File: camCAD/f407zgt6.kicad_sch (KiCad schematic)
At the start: 2 parts, among them J2 SWD Header, U3 STM32F407ZGTx

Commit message: miscellaneous changes
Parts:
- removed J2: SWD Header, symbol Connector:Conn_01x02_Pin
- added J2: JTAG header, symbol Connector:Conn_01x10_Pin
- added R1: R_US, symbol Device:R_US
- added SW2: SW_Push, symbol Switch:SW_Push
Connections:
- net PDR_ON is gone; now on net VDD1: U3.143 (PDR_ON)
- net BOOT0: now also R1.1, SW2.2
- net NRST: now also J2.10 (Pin_10)
- net PB3: now also J2.6 (Pin_6)
- net VDD1: now also J2.1 (Pin_1)
- net PA13: now reaches U3.105 (PA13)
- net PA13: now also J2.2 (Pin_2)
- net PA14: now reaches U3.109 (PA14)
- net PA14: now also J2.4 (Pin_4)
- net PA15: now reaches U3.110 (PA15)
- net PA15: now also J2.8 (Pin_8)
- net PA5: now reaches U3.41 (PA5)
- net PB11: now reaches U3.70 (PB11)
- net PD1: no longer names the net of U3.115 (PD1)
- net PD2: no longer names the net of U3.116 (PD2)
- new net GND: J2.3 (Pin_3), J2.5 (Pin_5), J2.9 (Pin_9), R1.2
- new net SC_3V3: SW2.1
- no-connect marks 0 -> 81
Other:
- note added: "ARM10-compatible connector (JTAG)"
- note added: "Bootloader mode switch"
- note added: "JCLK"
- note added: "JRCLK"
- note added: "JTDI"
- note added: "JTDO"
- note added: "JTMS"
- note added: "NRST"
- note added: "VCC"
- note removed: "SWCLK"
- note removed: "SWDIO"

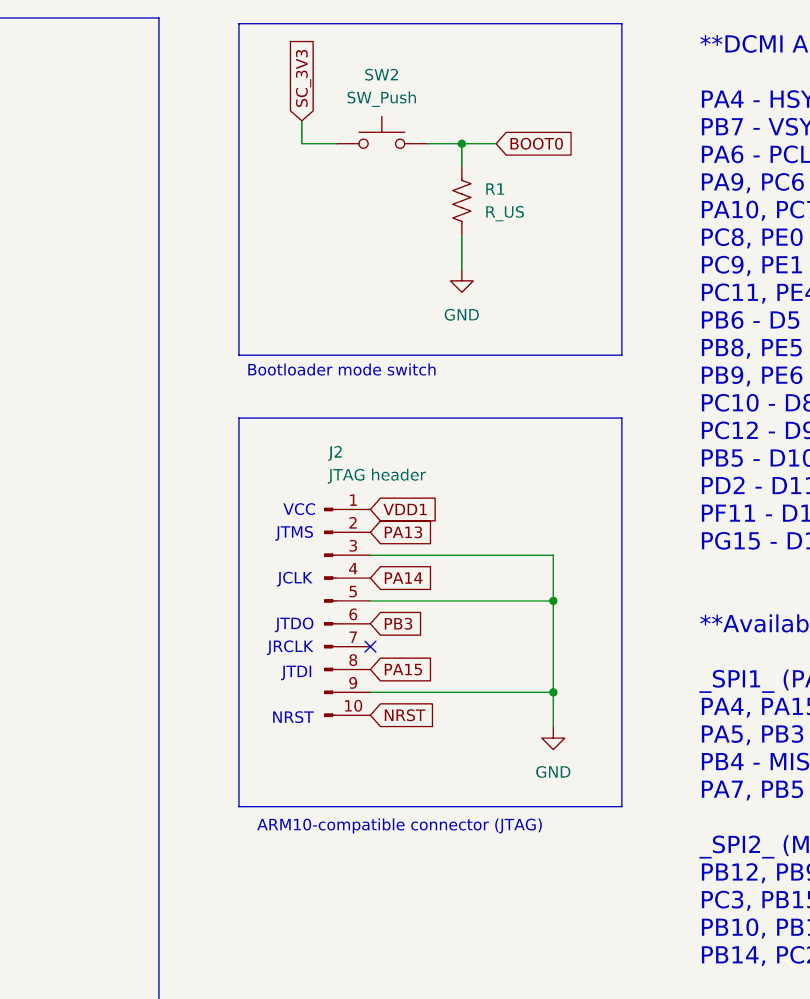
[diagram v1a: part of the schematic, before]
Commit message: Added footprints for major components, renamed some components for more specific information
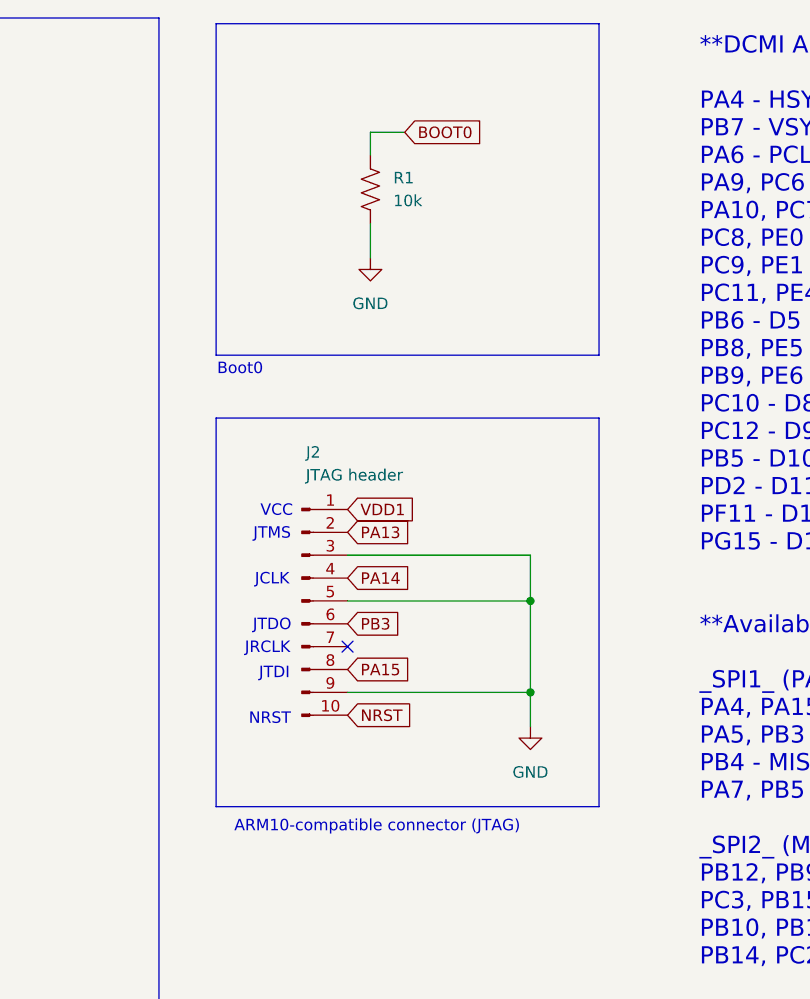
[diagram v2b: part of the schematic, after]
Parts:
- removed SW2: SW_Push, symbol Switch:SW_Push
- J2: footprint (none) -> 1_Headers:SULLINS_SBH11-PBPC-D05-ST-BK
- R1: value R_US -> 10k
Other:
- note added: "Boot0"
- note removed: "Bootloader mode switch"
- moved on the sheet: J2, R1

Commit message: Started PCB Layout, need to add a user interface
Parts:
- R1: footprint (none) -> Resistor_SMD:R_0402_1005Metric
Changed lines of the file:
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@@
 			)
 		)
-		(property "Footprint" ""
+		(property "Footprint" "Resistor_SMD:R_0402_1005Metric"
 			(at 161.036 34.544 90)
 			(hide yes)

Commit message: Added user interface schematic and updated "camCAD/README.md"
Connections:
- net PF3: now reaches U3.13 (PF3)
- net PG1: now reaches U3.57 (PG1)
- net PG2: now reaches U3.87 (PG2)
- net PG3: now reaches U3.88 (PG3)
- net PG4: now reaches U3.89 (PG4)
- net PG5: now reaches U3.90 (PG5)
- no-connect marks 81 -> 75
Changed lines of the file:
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@@
+	)
+	(no_connect
+		(at 38.1 64.77)
 	)
 	(no_connect
@@
 	)
 	(no_connect
-		(at 38.1 69.85)
-	)
-	(no_connect
 		(at 38.1 189.23)
 	)
 	(no_connect
+		(at 38.1 128.27)
+	)
+	(no_connect
+		(at 104.14 191.77)
+	)
+	(no_connect
+		(at 104.14 135.89)
+	)
+	(no_connect
+		(at 104.14 156.21)
+	)
+	(no_connect
+		(at 38.1 80.01)
+	)
+	(no_connect
+		(at 104.14 125.73)
+	)
+	(no_connect
+		(at 104.14 105.41)
+	)
+	(no_connect
+		(at 38.1 82.55)
+	)
+	(no_connect
+		(at 38.1 59.69)
+	)
+	(no_connect
+		(at 104.14 128.27)
+	)
+	(no_connect
+		(at 104.14 207.01)
+	)
+	(no_connect
+		(at 104.14 102.87)
+	)
+	(no_connect
+		(at 104.14 148.59)
+	)
+	(no_connect
+		(at 104.14 176.53)
+	)
+	(no_connect
 		(at 38.1 118.11)
 	)
 	(no_connect
-		(at 38.1 128.27)
-	)
-	(no_connect
-		(at 104.14 191.77)
-	)
-	(no_connect
-		(at 38.1 77.47)
-	)
-	(no_connect
-		(at 38.1 67.31)
-	)
-	(no_connect
-		(at 104.14 135.89)
-	)
-	(no_connect
-		(at 104.14 156.21)
-	)
-	(no_connect
-		(at 38.1 80.01)
-	)
-	(no_connect
-		(at 104.14 125.73)
-	)
-	(no_connect
-		(at 104.14 105.41)
-	)
-	(no_connect
-		(at 38.1 82.55)
-	)
-	(no_connect
-		(at 38.1 59.69)
-	)
-	(no_connect
-		(at 104.14 128.27)
-	)
-	(no_connect
-		(at 104.14 207.01)
-	)
-	(no_connect
-		(at 104.14 102.87)
-	)
-	(no_connect
-		(at 38.1 115.57)
-	)
-	(no_connect
-		(at 104.14 148.59)
-	)
-	(no_connect
-		(at 104.14 176.53)
-	)
-	(no_connect
 		(at 38.1 85.09)
 	)
 	(no_connect
-		(at 38.1 72.39)
-	)
-	(no_connect
 		(at 38.1 100.33)
 	)
@@
 	)
 	(no_connect
+		(at 38.1 135.89)
+	)
+	(no_connect
+		(at 104.14 186.69)
+	)
+	(no_connect
+		(at 38.1 140.97)
+	)
+	(no_connect
+		(at 38.1 179.07)
+	)
+	(no_connect
+		(at 38.1 138.43)
+	)
+	(no_connect
+		(at 104.14 168.91)
+	)
+	(no_connect
+		(at 104.14 151.13)
+	)
+	(no_connect
+		(at 38.1 158.75)
+	)
+	(no_connect
+		(at 104.14 163.83)
+	)
+	(no_connect
+		(at 38.1 95.25)
+	)
+	(no_connect
+		(at 38.1 57.15)
+	)
+	(no_connect
+		(at 104.14 67.31)
+	)
+	(no_connect
+		(at 38.1 184.15)
+	)
+	(no_connect
+		(at 104.14 194.31)
+	)
+	(no_connect
 		(at 38.1 120.65)
-	)
-	(no_connect
-		(at 38.1 135.89)
-	)
-	(no_connect
-		(at 104.14 186.69)
-	)
-	(no_connect
-		(at 38.1 140.97)
-	)
-	(no_connect
-		(at 38.1 179.07)
-	)
-	(no_connect
-		(at 38.1 138.43)
-	)
-	(no_connect
-		(at 104.14 168.91)
-	)
-	(no_connect
-		(at 104.14 151.13)
-	)
-	(no_connect
-		(at 38.1 158.75)
-	)
-	(no_connect
-		(at 104.14 163.83)
-	)
-	(no_connect
-		(at 38.1 74.93)
-	)
-	(no_connect
-		(at 38.1 95.25)
-	)
-	(no_connect
-		(at 38.1 57.15)
-	)
-	(no_connect
-		(at 104.14 67.31)
-	)
-	(no_connect
-		(at 38.1 184.15)
-	)
-	(no_connect
-		(at 104.14 194.31)
-	)
-	(no_connect
-		(at 38.1 64.77)
 	)
 	(wire
@@
 		)
 	)
+	(global_label "PG4"
+		(shape input)
+		(at 38.1 74.93 180)
+		(fields_autoplaced yes)
+		(effects
+			(font
+				(size 1.27 1.27)
+			)
+			(justify right)
+		)
+		(property "Intersheetrefs" "${INTERSHEET_REFS}"
+			(at 31.3653 74.93 0)
+			(hide yes)
+			(show_name no)
+			(do_not_autoplace no)
+			(effects
+				(font
+					(size 1.27 1.27)
+				)
+				(justify right)
+			)
+		)
+	)
 	(global_label "VDD11"
 		(shape input)
@@
 		)
 	)
+	(global_label "PG1"
+		(shape input)
+		(at 38.1 67.31 180)
+		(fields_autoplaced yes)
+		(effects
+			(font
+				(size 1.27 1.27)
+			)
+			(justify right)
+		)
+		(property "Intersheetrefs" "${INTERSHEET_REFS}"
+			(at 31.3653 67.31 0)
+			(hide yes)
+			(show_name no)
+			(do_not_autoplace no)
+			(effects
+				(font
+					(size 1.27 1.27)
+				)
+				(justify right)
+			)
+		)
+	)
+	(global_label "PF3"
+		(shape input)
+		(at 38.1 115.57 180)
+		(fields_autoplaced yes)
+		(effects
+			(font
+				(size 1.27 1.27)
+			)
+			(justify right)
+		)
+		(property "Intersheetrefs" "${INTERSHEET_REFS}"
+			(at 31.5467 115.57 0)
+			(hide yes)
+			(show_name no)
+			(do_not_autoplace no)
+			(effects
+				(font
+					(size 1.27 1.27)
+				)
+				(justify right)
+			)
+		)
+	)
 	(global_label "VDD1"
 		(shape input)
@@
 		)
 	)
+	(global_label "PG5"
+		(shape input)
+		(at 38.1 77.47 180)
+		(fields_autoplaced yes)
+		(effects
+			(font
+				(size 1.27 1.27)
+			)
+			(justify right)
+		)
+		(property "Intersheetrefs" "${INTERSHEET_REFS}"
+			(at 31.3653 77.47 0)
+			(hide yes)
+			(show_name no)
+			(do_not_autoplace no)
+			(effects
+				(font
+					(size 1.27 1.27)
+				)
+				(justify right)
+			)
+		)
+	)
+	(global_label "PG3"
+		(shape input)
+		(at 38.1 72.39 180)
+		(fields_autoplaced yes)
+		(effects
+			(font
+				(size 1.27 1.27)
+			)
+			(justify right)
+		)
+		(property "Intersheetrefs" "${INTERSHEET_REFS}"
+			(at 31.3653 72.39 0)
+			(hide yes)
+			(show_name no)
+			(do_not_autoplace no)
+			(effects
+				(font
+					(size 1.27 1.27)
+				)
+				(justify right)
+			)
+		)
+	)
 	(global_label "PD14"
 		(shape input)
@@
 			)
 		)
+	)
+	(global_label "PG2"
+		(shape input)
+		(at 38.1 69.85 180)
+		(fields_autoplaced yes)
+		(effects
+			(font
+				(size 1.27 1.27)
+			)
+			(justify right)
+		)
+		(property "Intersheetrefs" "${INTERSHEET_REFS}"
+			(at 31.3653 69.85 0)
+			(hide yes)
+			(show_name no)
+			(do_not_autoplace no)
+			(effects
+				(font
+					(size 1.27 1.27)
+				)
+				(justify right)
+			)
+		)

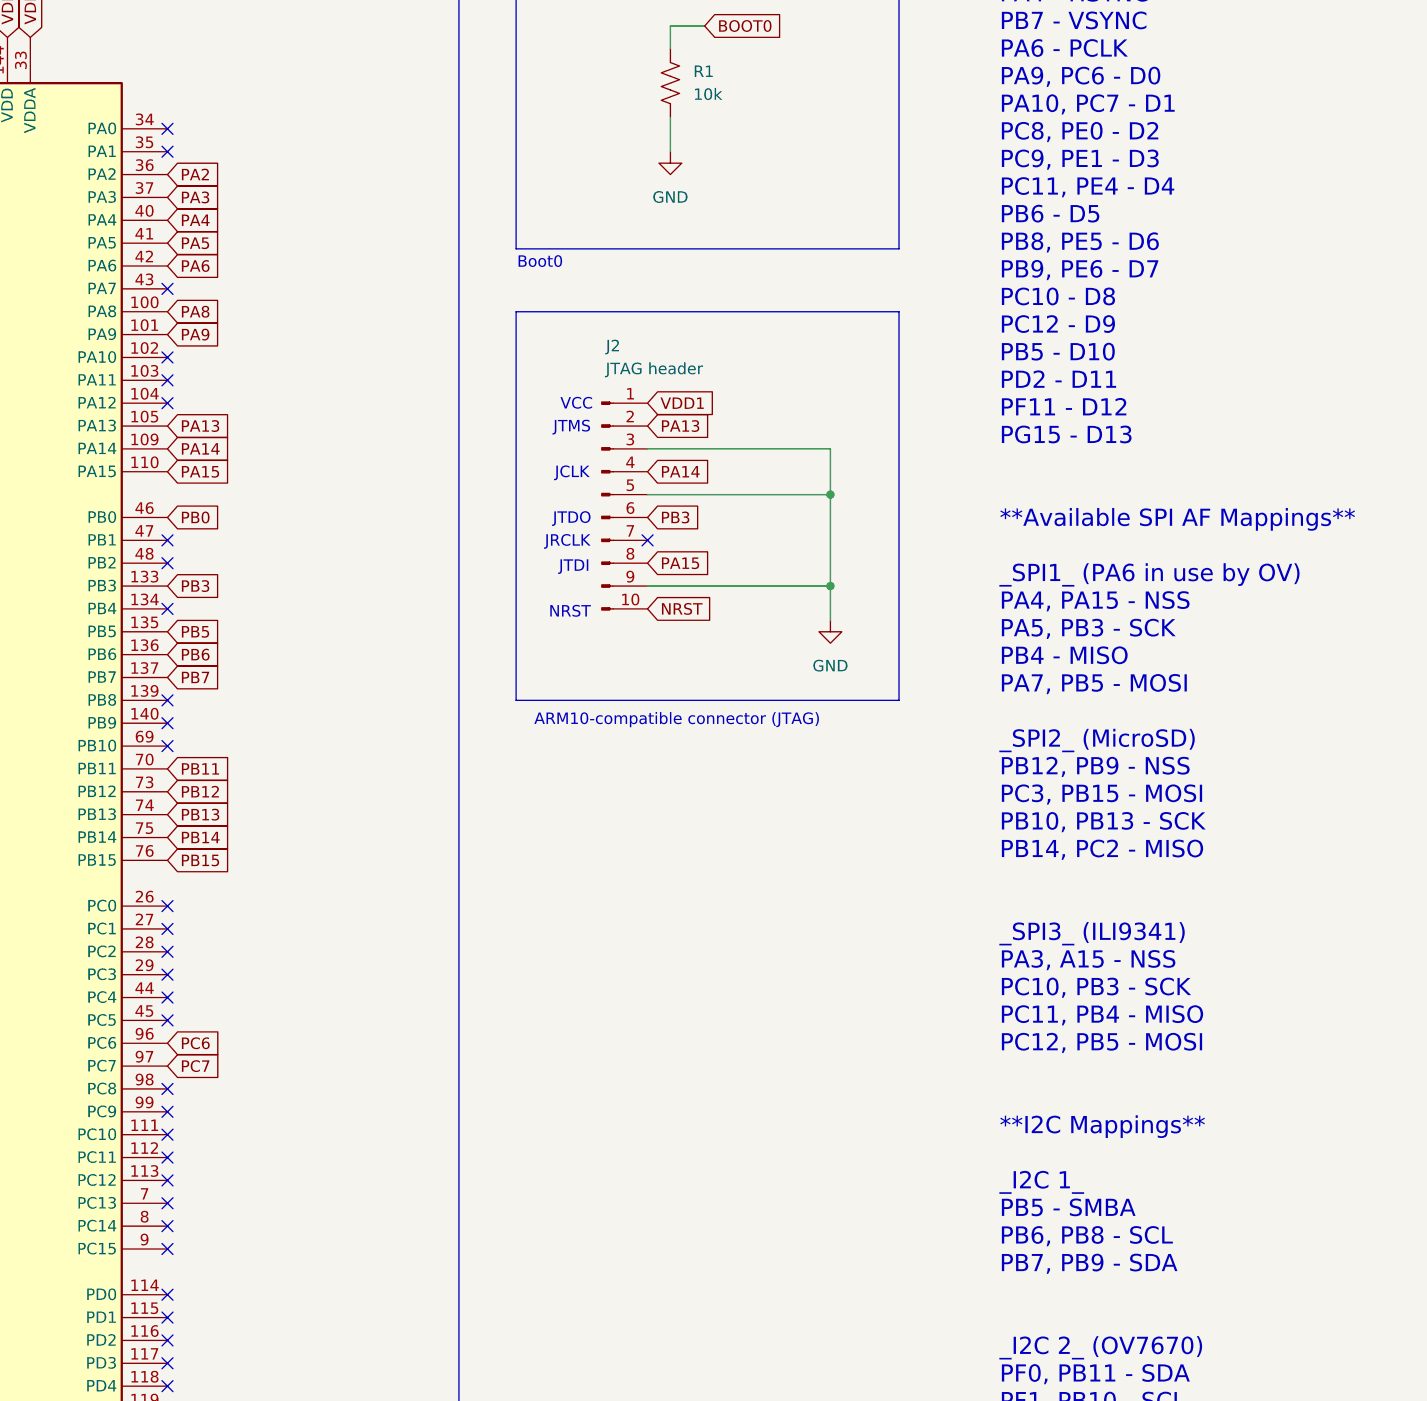
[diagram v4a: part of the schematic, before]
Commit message: REMADE with a much more suitable display
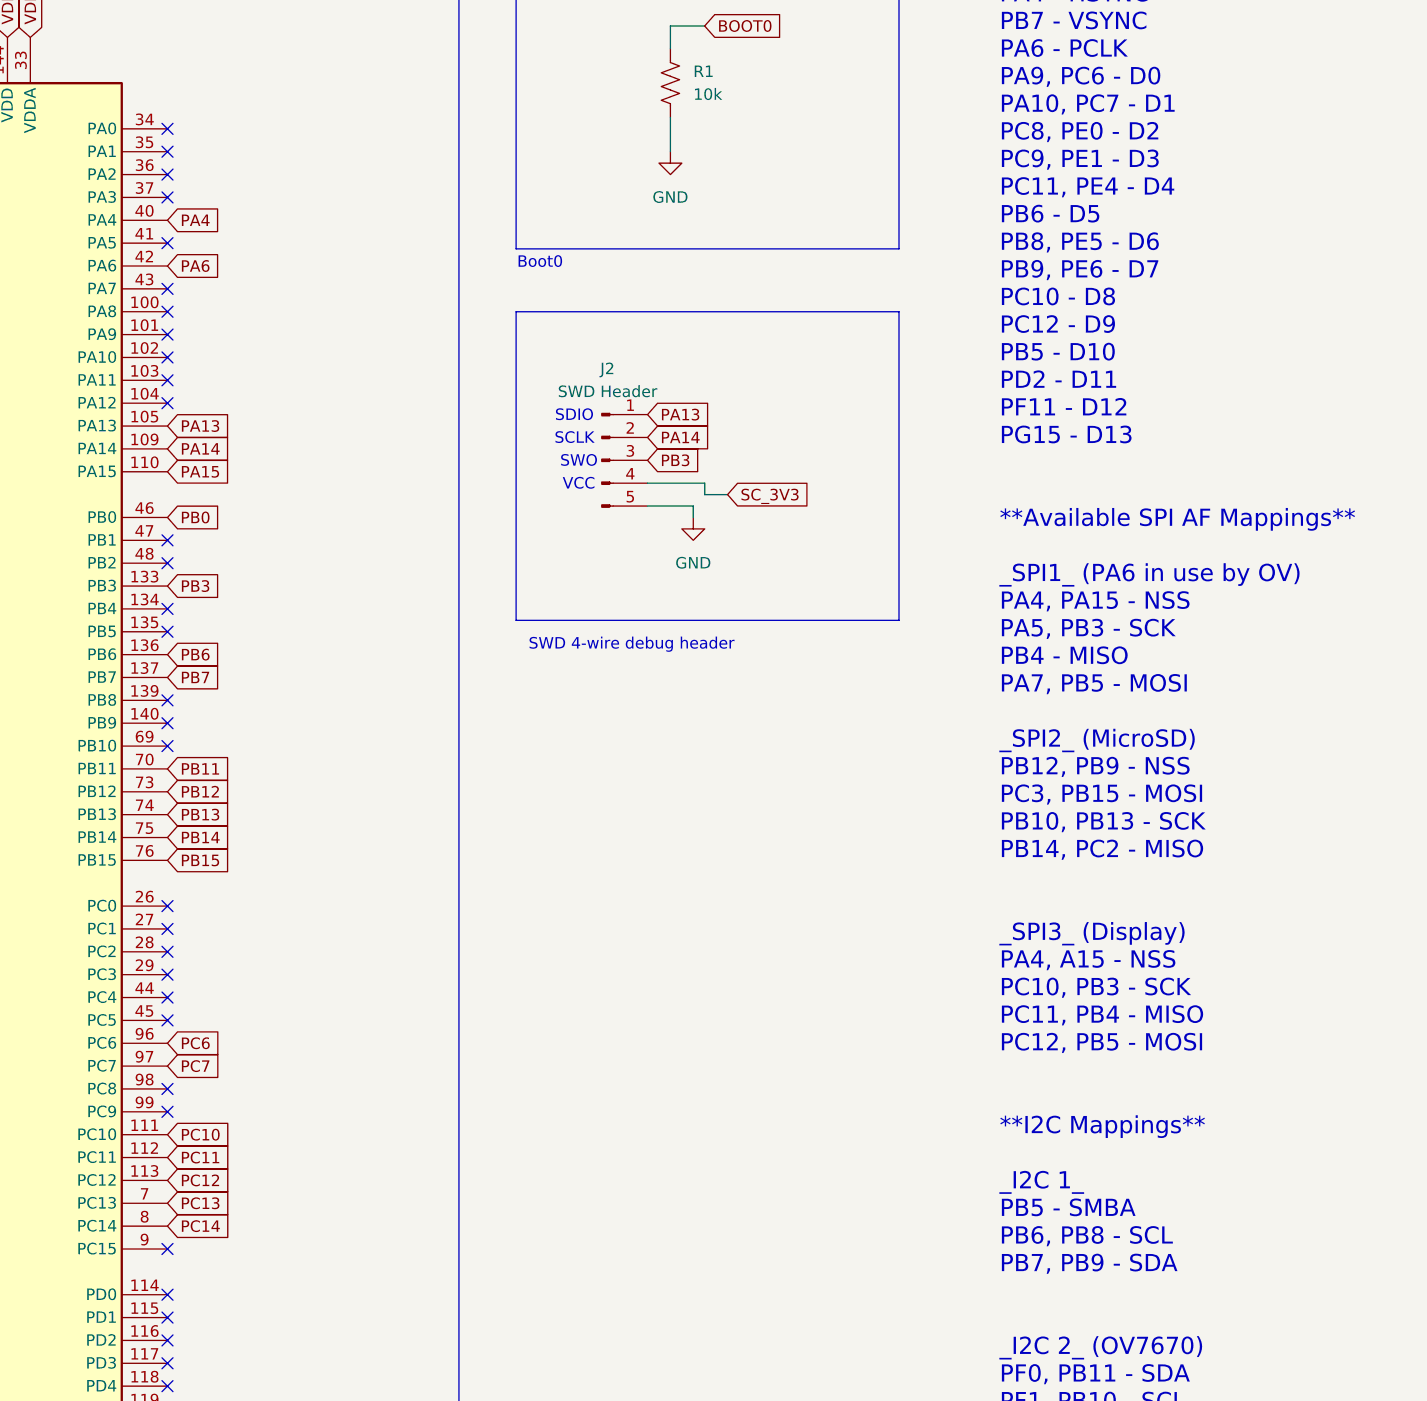
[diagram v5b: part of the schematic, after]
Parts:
- removed J2: JTAG header, 1_Headers:SULLINS_SBH11-PBPC-D05-ST-BK, symbol Connector:Conn_01x10_Pin
- added J2: SWD Header, Connector_PinHeader_2.54mm:PinHeader_1x05_P2.54mm_Vertical, symbol Connector:Conn_01x05_Pin
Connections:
- net GND: now also J2.5 (Pin_5)
- net PA13: now also J2.1 (Pin_1)
- net PA14: now also J2.2 (Pin_2)
- net PB3: now also J2.3 (Pin_3)
- net PC10: now reaches U3.111 (PC10)
- net PC11: now reaches U3.112 (PC11)
- net PC12: now reaches U3.113 (PC12)
- net PC13: now reaches U3.7 (PC13)
- net PC14: now reaches U3.8 (PC14)
- net PA2: no longer names the net of U3.36 (PA2)
- net PA3: no longer names the net of U3.37 (PA3)
- net PA5: no longer names the net of U3.41 (PA5)
- net PA8: no longer names the net of U3.100 (PA8)
- net PA9: no longer names the net of U3.101 (PA9)
- net PB5: no longer names the net of U3.135 (PB5)
- new net SC_3V3: J2.4 (Pin_4)
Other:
- note added: "SCLK"
- note added: "SDIO"
- note added: "SWD 4-wire debug header"
- note added: "SWO"
- note removed: "ARM10-compatible connector (JTAG)"
- note removed: "JCLK"
- note removed: "JRCLK"
- note removed: "JTDI"
- note removed: "JTDO"
- note removed: "JTMS"
- note removed: "NRST"
